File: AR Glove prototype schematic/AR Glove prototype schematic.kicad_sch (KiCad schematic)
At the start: 2 parts, among them U1 CY8C52??AXI-LP

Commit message: test upload
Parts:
- removed U1: CY8C52??AXI-LP, symbol Cypress_PSoC:CY8C52??AXI-LP
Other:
- moved on the sheet: A1

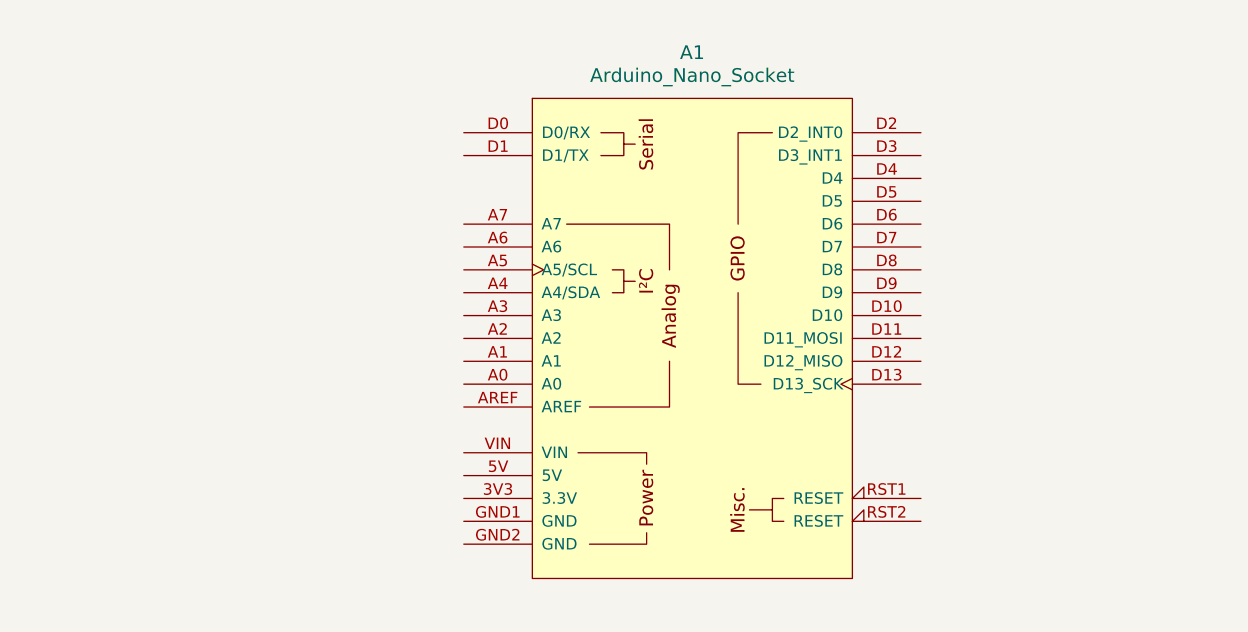
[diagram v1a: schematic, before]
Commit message: Update AR Glove prototype schematic.kicad_sch
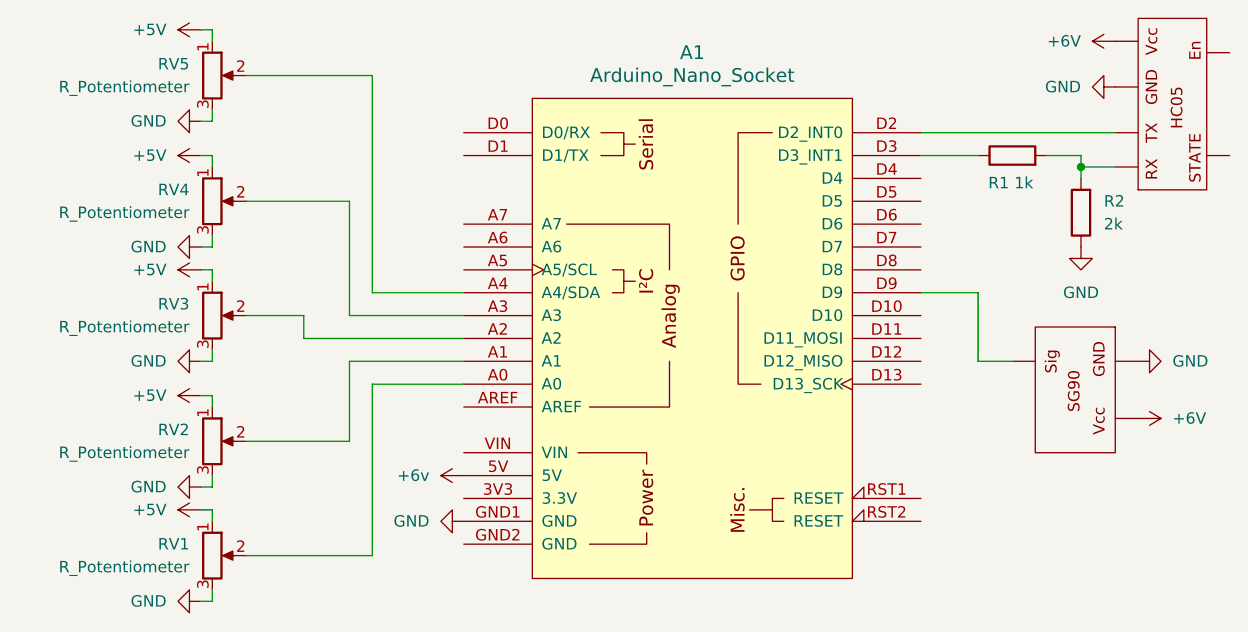
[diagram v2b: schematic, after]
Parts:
- added R1: 1k, symbol Device:R
- added R2: 2k, symbol Device:R
- added RV1, RV2, RV3, RV4, RV5: R_Potentiometer, symbol Device:R_Potentiometer
- added U1: ~, symbol customslibrary:sg90
- added U2: ~, symbol customslibrary:hc05_module
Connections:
- net +6v: now reaches A1.5V
- net at A1.A0: now also RV1.2
- net at A1.A1: now also RV2.2
- net at A1.A2: now also RV3.2
- net at A1.A3: now also RV4.2
- net at A1.A4 (A4/SDA): now also RV5.2
- net at A1.D2 (D2_INT0): now also U2.
- net at A1.D3 (D3_INT1): now also R1.1
- net at A1.D9: now also U1.
- net GND: now reaches A1.GND1 (GND)
- net GND: now also R2.1, RV1.3, RV2.3, RV3.3, RV4.3, RV5.3, U1., U2.
- new net: R1.2, R2.2, U2.
- new net +5V: RV1.1, RV2.1, RV3.1, RV4.1, RV5.1
- new net +6V: U1., U2.
